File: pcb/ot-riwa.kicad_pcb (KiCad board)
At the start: 2 copper layers, 70 x 61.8 mm, 19 parts, among them IC2 RV-3028-C7, J1 USB4105-GF-A, U1 DPS368XTSA1, U2 MS88SF2, U3 MCP73831/OT, U4 AP2112K-3.3

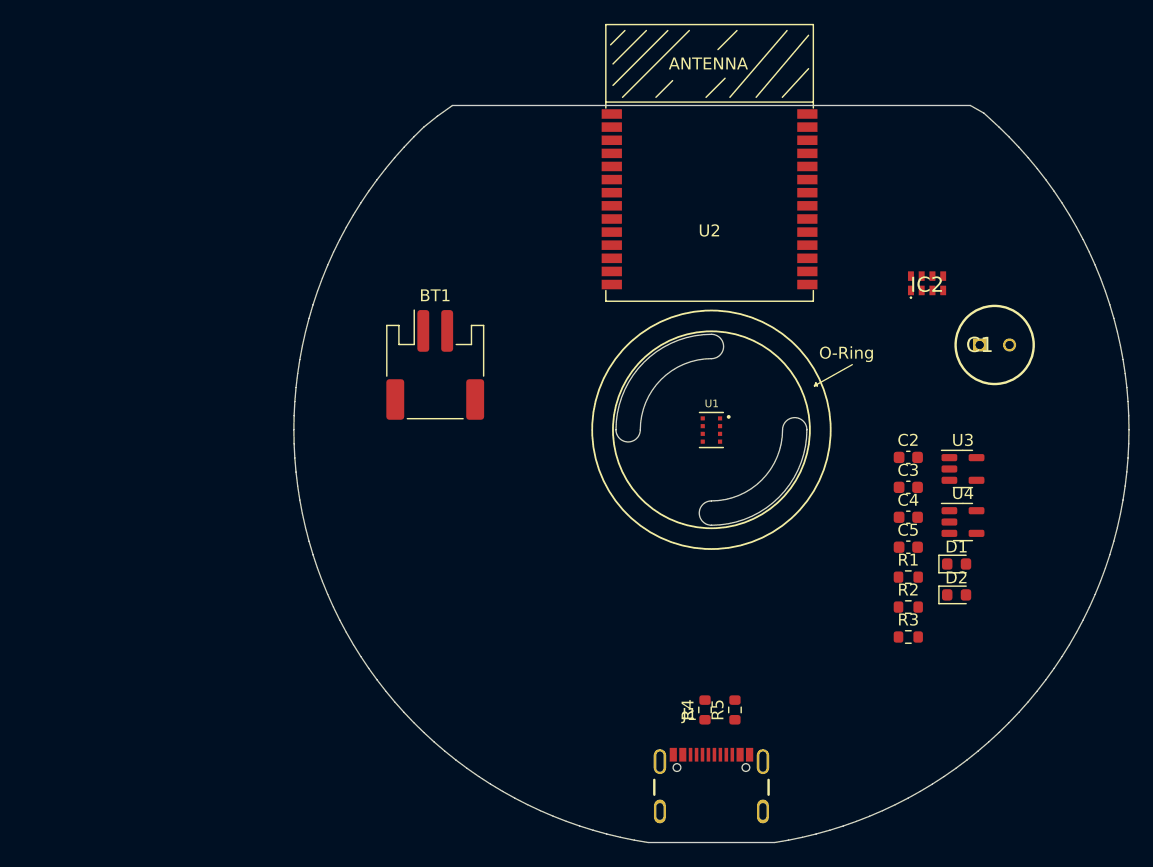
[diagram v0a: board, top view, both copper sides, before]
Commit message: Placed components on PCB Board (no layouting)
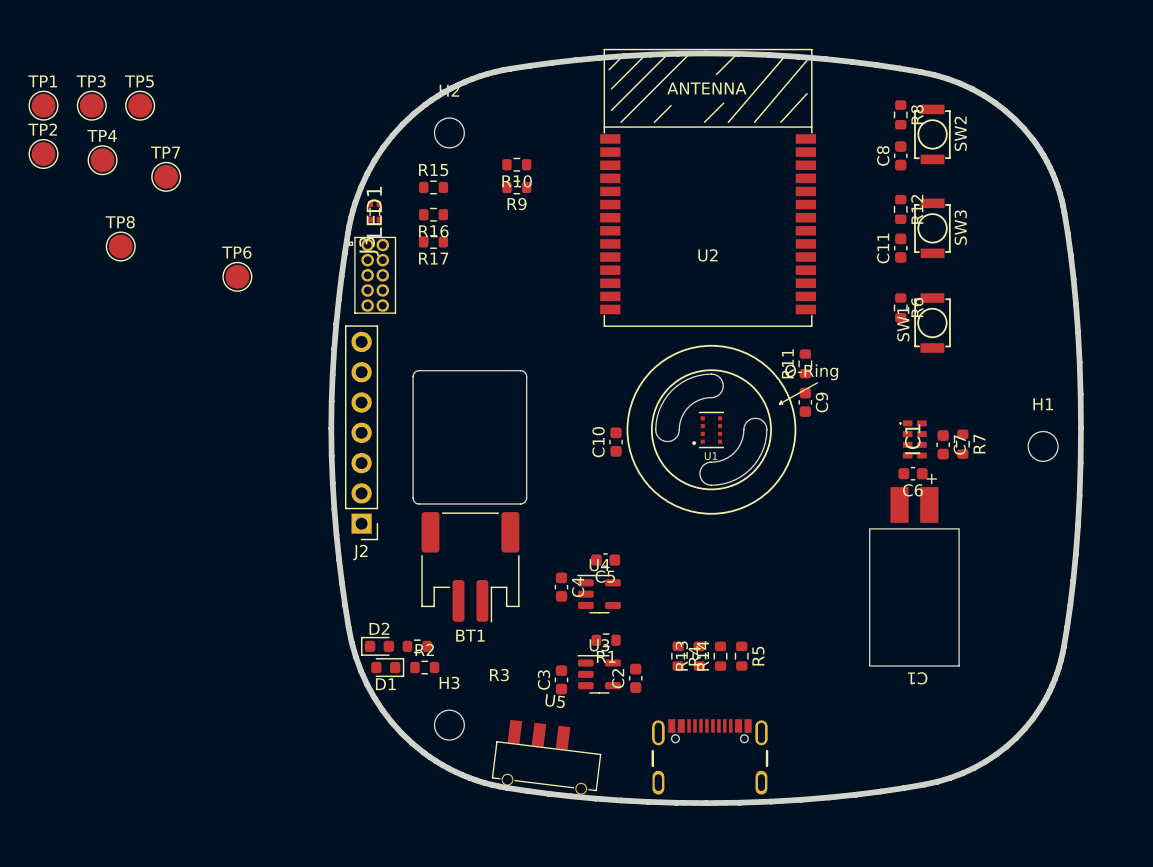
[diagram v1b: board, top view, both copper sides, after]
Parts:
- removed IC2: RV-3028-C7, RV-3028-C7:RV3028C732768kHz1ppmTAQC
- added C10: 0.1uF, Capacitor_SMD:C_0603_1608Metric, F.Cu at (128.3, 96.7)
- added C11: 0.1uF, Capacitor_SMD:C_0603_1608Metric, F.Cu at (152.1, 80.4)
- added C6: 0.1uF, Capacitor_SMD:C_0603_1608Metric, F.Cu at (153.2, 99.3)
- added C7: 0.1uF, Capacitor_SMD:C_0603_1608Metric, F.Cu at (155.7, 96.9)
- added C8: 0.1uF, Capacitor_SMD:C_0603_1608Metric, F.Cu at (152.1, 72.7)
- added C9: 0.1uF, Capacitor_SMD:C_0603_1608Metric, F.Cu at (144.1, 93.3)
- added G1: LOGO, LOGO, B.Cu at (136.3, 121.2)
- added H1: MountingHole, MountingHole:MountingHole_2.5mm, F.Cu at (164.1, 97.0)
- added H2: MountingHole, MountingHole:MountingHole_2.5mm, F.Cu at (114.3, 70.7)
- added H3: MountingHole, MountingHole:MountingHole_2.5mm, F.Cu at (114.3, 120.4)
- added IC1: RV-3028-C7, RV-3028-C7:RV3028C732768kHz1ppmTAQC, F.Cu at (153.3, 96.4)
- added J2: Conn_01x07_Pin, Connector_PinHeader_2.54mm:PinHeader_1x07_P2.54mm_Vertical, F.Cu at (106.9, 103.5)
- added J3: 62201021121, 62201021121:WURTH-1.27MM-PITCH-2WAY, F.Cu at (108.1, 82.7)
- added LED1: APHF1608LSEEQBDZGKC, APHF1608LSEEQBDZGKC:APHF1608LSEEQBDZGKC, F.Cu at (108.0, 77.4)
- added R10: 10k, Resistor_SMD:R_0603_1608Metric, F.Cu at (120.0, 73.4)
- added R11: 10k, Resistor_SMD:R_0603_1608Metric, F.Cu at (144.1, 90.1)
- added R12: 10k, Resistor_SMD:R_0603_1608Metric, F.Cu at (152.1, 77.2)
- added R13: 0R, Resistor_SMD:R_0603_1608Metric, F.Cu at (135.3, 114.6)
- added R14: 0R, Resistor_SMD:R_0603_1608Metric, F.Cu at (137.0, 114.6)
- added R15: 1k2, Resistor_SMD:R_0603_1608Metric, F.Cu at (113.0, 75.3)
- added R16: 2k2, Resistor_SMD:R_0603_1608Metric, F.Cu at (113.0, 77.6)
- added R17: 390R, Resistor_SMD:R_0603_1608Metric, F.Cu at (113.0, 79.9)
- added R6: 10k, Resistor_SMD:R_0603_1608Metric, F.Cu at (152.1, 85.4)
- added R7: 10k, Resistor_SMD:R_0603_1608Metric, F.Cu at (157.4, 96.8)
- added R8: 10k, Resistor_SMD:R_0603_1608Metric, F.Cu at (152.1, 69.2)
- added R9: 10k, Resistor_SMD:R_0603_1608Metric, F.Cu at (120.0, 75.3)
- added SW1: SKRKAEE020, SKRKAEE020:SKRKAEE020, F.Cu at (154.8, 86.7)
- added SW2: SKRKAEE020, SKRKAEE020:SKRKAEE020, F.Cu at (154.8, 70.9)
- added SW3: SKRKAEE020, SKRKAEE020:SKRKAEE020, F.Cu at (154.8, 78.7)
- added TP1: TP_3V3, TestPoint:TestPoint_Pad_D2.0mm, F.Cu at (80.3, 68.5)
- added TP2: TP_GND, TestPoint:TestPoint_Pad_D2.0mm, F.Cu at (80.3, 72.5)
- added TP3: TP_SDA, TestPoint:TestPoint_Pad_D2.0mm, F.Cu at (84.3, 68.5)
- added TP4: TP_SCK, TestPoint:TestPoint_Pad_D2.0mm, F.Cu at (85.2, 73.0)
- added TP5: TP_RTC_INT, TestPoint:TestPoint_Pad_D2.0mm, F.Cu at (88.4, 68.5)
- added TP6: TP_DPS_INT, TestPoint:TestPoint_Pad_D2.0mm, F.Cu at (96.5, 82.8)
- added TP7: TP_VBACKUP, TestPoint:TestPoint_Pad_D2.0mm, F.Cu at (90.6, 74.4)
- added TP8: TP_ENABLE, TestPoint:TestPoint_Pad_D2.0mm, F.Cu at (86.7, 80.3)
- added U5: 450405020524, 450405020524:450405020524, F.Cu at (122.3, 125.4)
- C1: footprint JUWT1105MCD:CAPPRD250W50D655H1050 -> JUWT1105MCD:supercap_horizontal
- moved D1 48.6 mm to (109.0, 115.6), turned to 180 degrees
- moved D2 48.6 mm to (108.4, 113.8)
- moved R3 41.2 mm to (111.6, 113.8), turned to 180 degrees
- moved R2 40.9 mm to (112.2, 115.6)
- moved U3 35.0 mm to (126.9, 116.1)
- moved C3 33.3 mm to (123.7, 116.6), turned to 90 degrees
- moved U4 31.1 mm to (126.9, 109.4)
- moved C4 29.7 mm to (123.7, 108.8), turned to -90 degrees
- moved C2 29.4 mm to (129.9, 116.5), turned to 90 degrees
- moved R1 25.9 mm to (127.4, 113.3), turned to 180 degrees
- moved C5 25.4 mm to (127.4, 106.6), turned to 180 degrees
- moved C1 18.2 mm to (153.5, 105.9), turned to 180 degrees
- moved BT1 17.2 mm to (116.1, 107.1), turned to 180 degrees
- moved R4 5.04 mm to (133.5, 114.6), turned to -90 degrees
- moved R5 4.54 mm to (138.8, 114.6), turned to -90 degrees
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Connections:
- net /main/USB_D+ renamed /main/MCU/USB_D+
- net /main/USB_D- renamed /main/MCU/USB_D-
- C1 pad 1: unconnected-(C1-+-Pad1) -> /main/RTC/VBackup
- C1 pad 2: unconnected-(C1---Pad2) -> GND
- U1 pad 1: Net-(U1-GND-Pad1) -> GND
- U1 pad 3: unconnected-(U1-SDI-Pad3) -> /main/SDA
- U1 pad 4: unconnected-(U1-SCK-Pad4) -> /main/SCK
- U1 pad 5: unconnected-(U1-SDO-Pad5) -> /main/DPS_INT
- U1 pad 6: unconnected-(U1-VDDIO-Pad6) -> +3.3V
- U1 pad 7: Net-(U1-GND-Pad1) -> GND
- U1 pad 8: unconnected-(U1-VDD-Pad8) -> +3.3V
- U2 pad 1: unconnected-(U2-GND-Pad1) -> GND
- U2 pad 10: unconnected-(U2-P0.08-Pad10) -> /main/MCU/LED_BLUE
- U2 pad 11: unconnected-(U2-P1.09-Pad11) -> /main/DPS_INT
- U2 pad 12: unconnected-(U2-P0.12-Pad12) -> /main/~{RTC_INT}
- U2 pad 13: unconnected-(U2-GND1-Pad13) -> GND
- U2 pad 14: unconnected-(U2-VCC-Pad14) -> +3.3V
- U2 pad 17: unconnected-(U2-SWDCLK-Pad17) -> /main/MCU/SWDCLK
- U2 pad 18: unconnected-(U2-SWDIO-Pad18) -> /main/MCU/SWDIO
- U2 pad 2: unconnected-(U2-P1.13-Pad2) -> /main/SCK
- U2 pad 22: unconnected-(U2-P0.20-Pad22) -> /main/MCU/BTN
- U2 pad 23: unconnected-(U2-P0.18/RST-Pad23) -> /main/MCU/RESET
- U2 pad 26: unconnected-(U2-D+-Pad26) -> /main/MCU/D+
- U2 pad 27: unconnected-(U2-D--Pad27) -> /main/MCU/D-
- U2 pad 28: unconnected-(U2-VDDH-Pad28) -> +3.3V
- U2 pad 3: unconnected-(U2-P1.15-Pad3) -> /main/SDA
- U2 pad 4: unconnected-(U2-P0.02-Pad4) -> /main/MCU/Rx
- U2 pad 5: unconnected-(U2-P0.29-Pad5) -> /main/MCU/Tx
- U2 pad 8: unconnected-(U2-P0.04-Pad8) -> /main/MCU/LED_RED
- U2 pad 9: unconnected-(U2-P0.06-Pad9) -> /main/MCU/LED_GREEN
- U4 pad 3: /main/ENABLE -> /main/PSU/ENABLE
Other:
- board size 70 x 61.8 mm -> 62.9 x 62.9 mm

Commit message: Replaces nRF52840 with ESP32-S3
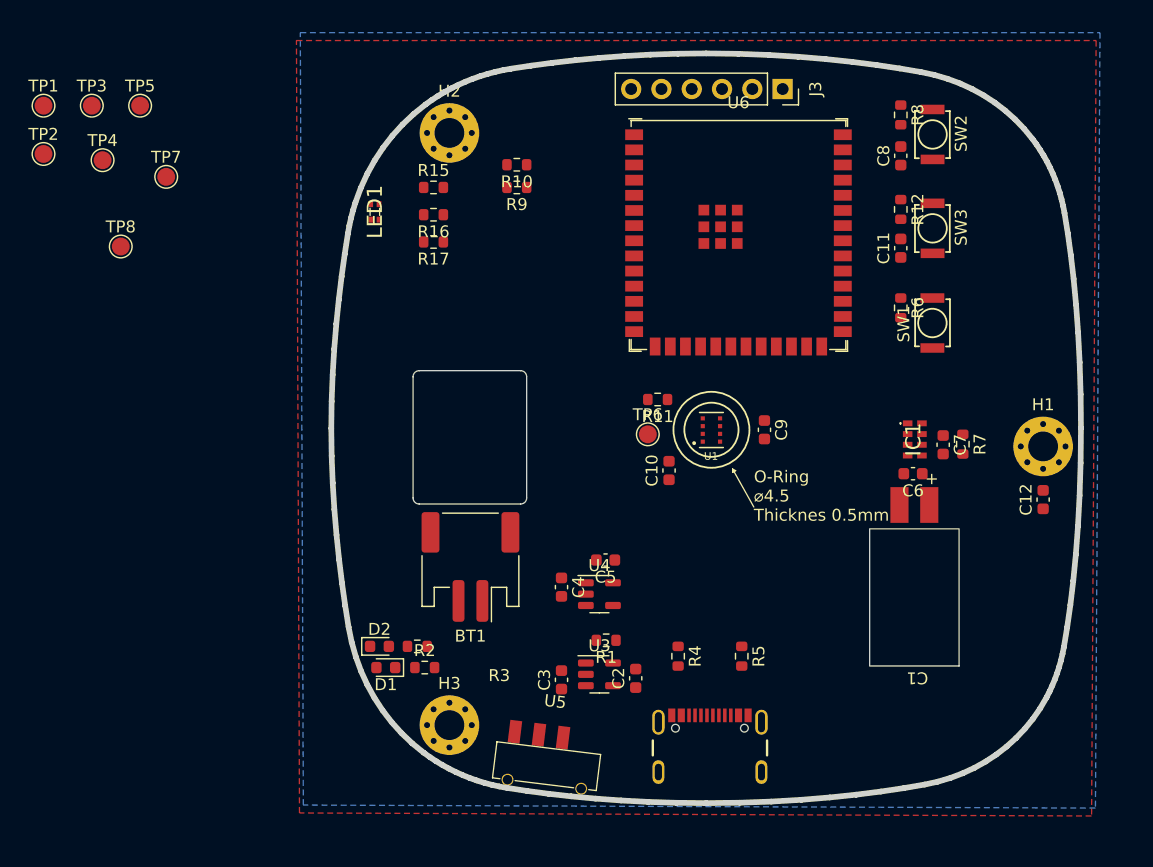
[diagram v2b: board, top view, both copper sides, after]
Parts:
- removed J2: Conn_01x07_Pin, Connector_PinHeader_2.54mm:PinHeader_1x07_P2.54mm_Vertical
- removed R13, R14: 0R, Resistor_SMD:R_0603_1608Metric
- removed U2: MS88SF2, MS88SF2:MS88SF2
- added C12: 0.1uF, Capacitor_SMD:C_0603_1608Metric, F.Cu at (164.1, 101.5)
- added U6: ESP32-S3-WROOM-1, ESP32-S3:ESP32-S3-WROOM-1U, F.Cu at (138.5, 79.2)
- H1, H2, H3: value MountingHole -> MountingHole_Pad; footprint MountingHole:MountingHole_2.5mm -> MountingHole:MountingHole_2.5mm_Pad_Via
- J3: value 62201021121 -> DNP; footprint 62201021121:WURTH-1.27MM-PITCH-2WAY -> Connector_PinSocket_2.54mm:PinSocket_1x06_P2.54mm_Vertical
- TP1, TP2, TP3, TP4, TP5, TP6, TP7, TP8: footprint TestPoint:TestPoint_Pad_D2.0mm -> TestPoint:TestPoint_Pad_D1.5mm
- moved J3 37.6 mm to (142.2, 67.1)
- moved TP6 36.9 mm to (130.9, 96.0)
- moved R11 12.7 mm to (131.8, 93.1), turned to 180 degrees
- moved C10 5.05 mm to (132.7, 99.0)
- moved C9 4.13 mm to (140.7, 95.6)
- moved J1 0.89 mm to (136.1, 124.3)
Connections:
- D1 pad 2: +BATT -> VBUS
- J3 pad 2: /main/MCU/SWDIO -> GND
- J3 pad 3: GND -> /main/MCU/Tx
- J3 pad 4: /main/MCU/SWDCLK -> /main/MCU/Rx
- J3 pad 5: GND -> /main/MCU/GPIO0
- J3 pad 6: unconnected-(J3-Pad6) -> /main/MCU/RESET
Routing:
- added copper zone on B.Cu, net GND
- added copper zone on F.Cu, net GND
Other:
- outline, holes or cut-outs redrawn
- board text added: "O-Ring ⌀4.5 Thicknes 0.5mm"
- board text removed: "O-Ring"

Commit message: Layout all components
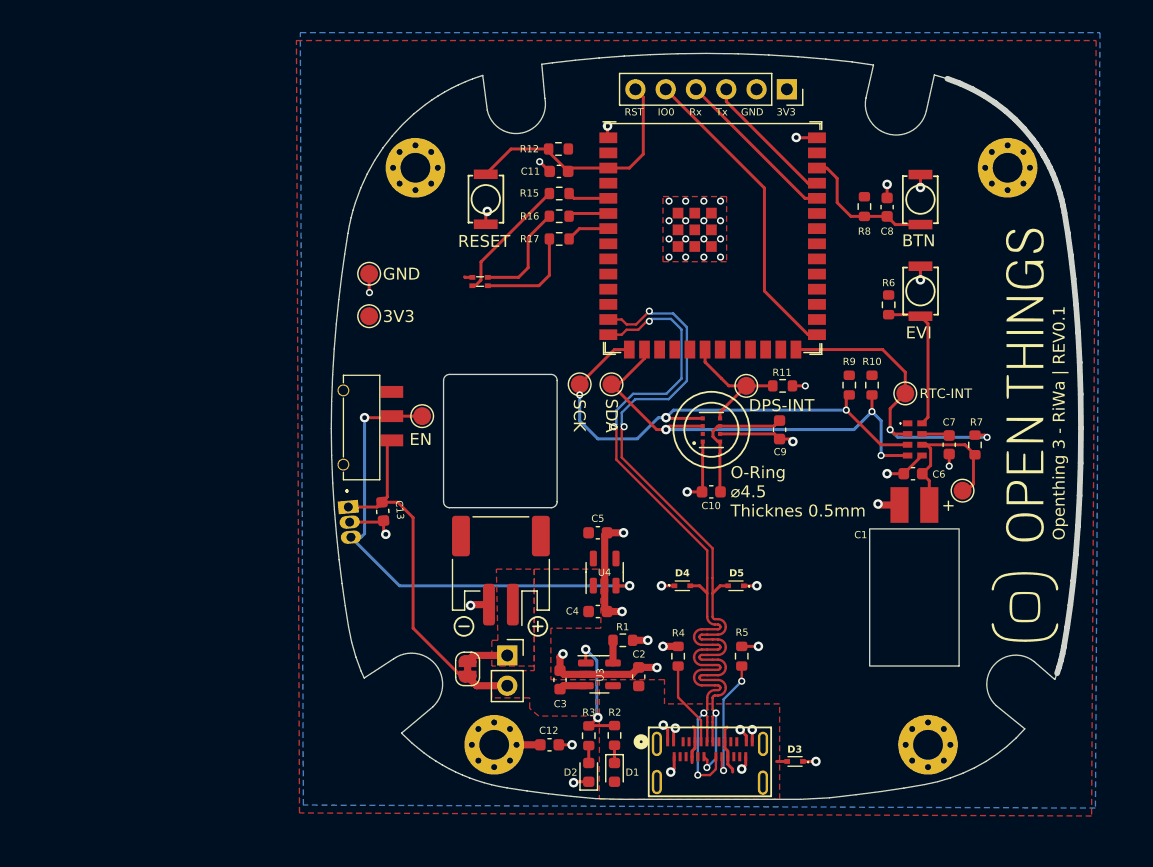
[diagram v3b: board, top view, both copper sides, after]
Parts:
- added C13: 0.1µF, Capacitor_SMD:C_0603_1608Metric, F.Cu at (108.7, 102.5)
- added D3: LESD5D5.0CT1G, LESD5D5.0CT1G:LESD5D50CT1G, F.Cu at (143.3, 123.4)
- added D4: LESD5D5.0CT1G, LESD5D5.0CT1G:LESD5D50CT1G, F.Cu at (133.8, 108.7)
- added D5: LESD5D5.0CT1G, LESD5D5.0CT1G:LESD5D50CT1G, F.Cu at (138.3, 108.7)
- added H4: MountingHole_Pad, MountingHole:MountingHole_2.5mm_Pad_Via, F.Cu at (154.4, 122.0)
- added IC2: DRV5032FB, DRV5032DULPGM:DRV5032DULPGM, F.Cu at (105.8, 102.1)
- added J2: DNP, Connector_PinSocket_2.54mm:PinSocket_1x02_P2.54mm_Vertical, F.Cu at (119.2, 114.6)
- added JP1: DNP, Jumper:SolderJumper-2_P1.3mm_Bridged_RoundedPad1.0x1.5mm, F.Cu at (115.8, 115.7)
- G1: moved to F.Cu
- J1: value USB4105-GF-A -> 124018612112A; footprint USB4105-GF-A:GCT_USB4105-GF-A -> 124018612112A:CONN_124018612112A_AMP
- moved TP7 71.8 mm to (157.3, 100.7)
- moved TP5 68.6 mm to (152.5, 92.6)
- moved H1 52.4 mm to (118.1, 122.0), turned to -90 degrees
- moved TP3 49.4 mm to (127.9, 91.8)
- moved H2 46.9 mm to (161.1, 73.7), turned to -90 degrees
- moved H3 46.8 mm to (111.5, 73.7), turned to -90 degrees
- moved C12 46.2 mm to (122.7, 122.0), turned to 0 degrees
- moved TP4 44.2 mm to (125.2, 91.8)
- moved SW3 37.5 mm to (117.3, 76.3), turned to -90 degrees
- moved G1 36.6 mm to (162.6, 95.6), turned to 90 degrees
- moved R10 35.0 mm to (149.7, 91.9), turned to 90 degrees
- moved U5 34.3 mm to (105.4, 95.5), turned to -90 degrees
- moved TP1 32.5 mm to (107.6, 86.1)
- moved R9 32.4 mm to (147.8, 91.9), turned to 90 degrees
- moved C11 29.4 mm to (123.5, 74.0), turned to 180 degrees
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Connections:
- BT1 pad 1: +BATT -> /main/PSU/BATTX+
- U6 pad 16: unconnected-(U6-GPIO46-Pad16) -> /main/SDA
- U6 pad 17: /main/MCU/LED_RED -> unconnected-(U6-GPIO9/TOUCH9/ADC1_CH8/FSPIHD/SUBSPIHD-Pad17)
- U6 pad 18: /main/MCU/LED_GREEN -> unconnected-(U6-GPIO10/TOUCH10/ADC1_CH9/FSPICS0/FSPIIO4/SUBSPICS0-Pad18)
- U6 pad 19: /main/MCU/LED_BLUE -> unconnected-(U6-GPIO11/TOUCH11/ADC2_CH0/FSPID/FSPIIO5/SUBSPID-Pad19)
- U6 pad 21: /main/~{RTC_INT} -> unconnected-(U6-GPIO13/TOUCH13/ADC2_CH2/FSPIQ/FSPIIO7/SUBSPIQ-Pad21)
- U6 pad 26: unconnected-(U6-GPIO45-Pad26) -> /main/~{RTC_INT}
- U6 pad 4: /main/SDA -> unconnected-(U6-GPIO4/TOUCH4/ADC1_CH3-Pad4)
- U6 pad 5: unconnected-(U6-GPIO5/TOUCH5/ADC1_CH4-Pad5) -> /main/MCU/LED_RED
- U6 pad 6: unconnected-(U6-GPIO6/TOUCH6/ADC1_CH5-Pad6) -> /main/MCU/LED_GREEN
- U6 pad 7: unconnected-(U6-GPIO7/TOUCH7/ADC1_CH6-Pad7) -> /main/MCU/LED_BLUE
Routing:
- net GND: track 0.00 -> 71.6 mm, vias 0 -> 50
- net /main/MCU/USB_D+: track 0.00 -> 71.2 mm, vias 0 -> 4
- net /main/MCU/USB_D-: track 0.00 -> 69.8 mm, vias 0 -> 4
- net /main/SCK: track 0.00 -> 43.2 mm, vias 0 -> 3
- net /main/PSU/ENABLE: track 0.00 -> 42.1 mm, vias 0 -> 2
- net /main/SDA: track 0.00 -> 39.3 mm, vias 0 -> 3
- net +BATT: track 0.00 -> 33.1 mm
- net /main/~{RTC_INT}: track 0.00 -> 26.4 mm, vias 0 -> 2
- net /main/MCU/GPIO0: track 0.00 -> 26.3 mm
- net /main/MCU/RESET: track 0.00 -> 21.3 mm
- net +3.3V: track 0.00 -> 14.4 mm
- net /main/RTC/VBackup: track 0.00 -> 14.4 mm
- net /main/MCU/Rx: track 0.00 -> 13.9 mm
- net /main/RTC/EVI: track 0.00 -> 12.2 mm
- net /main/MCU/BTN: track 0.00 -> 11.8 mm
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- added copper zone on F.Cu, net +3.3V
- added copper zone on F.Cu, net +BATT
- added copper zone on F.Cu, net /main/PSU/BATTX+
- added copper zone on F.Cu, net VBUS
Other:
- board size 62.9 x 62.9 mm -> 62.9 x 62.5 mm
- board text added: "3V3"
- board text added: "BTN"
- board text added: "DPS-INT"
- board text added: "EN"
- board text added: "EVI"
- board text added: "GND"
- board text added: "IO0"
- board text added: "Openthing 3 - RiWa | REV0.1"
- board text added: "RESET"
- board text added: "RST"
- board text added: "RTC-INT"
- board text added: "Rx"
- board text added: "SCK"
- board text added: "SDA"
- board text added: "Tx"

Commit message: Refactored layout + silkscreen + added I2C connector
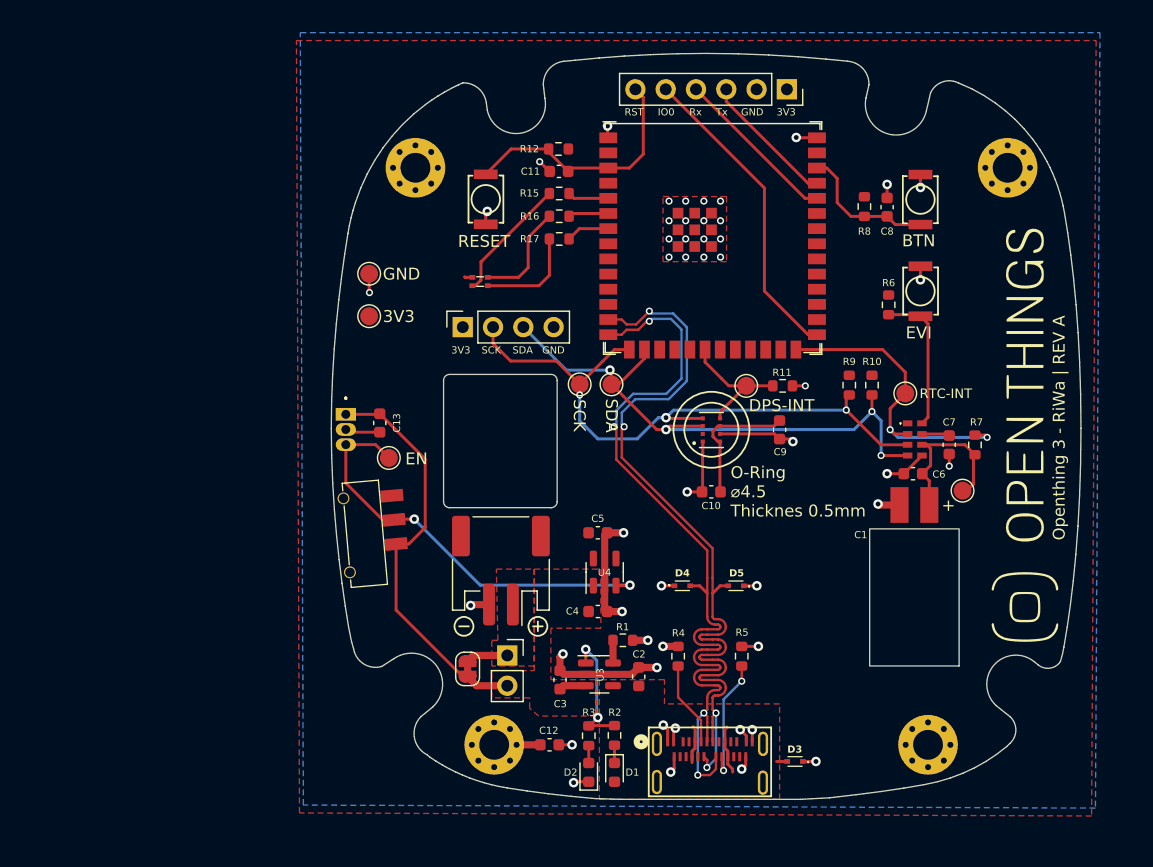
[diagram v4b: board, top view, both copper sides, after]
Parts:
- added J4: Conn_01x04_Pin, Connector_PinSocket_2.54mm:PinSocket_1x04_P2.54mm_Vertical, F.Cu at (115.4, 87.0)
- moved U5 9.05 mm to (105.7, 104.5), turned to -85 degrees
- moved IC2 7.78 mm to (105.6, 94.3), turned to 90 degrees
- moved C13 7.42 mm to (108.5, 95.1), turned to -90 degrees
- moved TP8 4.48 mm to (109.2, 98.0)
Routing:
- net /main/SCK: track 43.2 -> 53.3 mm
- net /main/SDA: track 39.3 -> 49.3 mm, vias 3 -> 4
- net /main/PSU/ENABLE: track 42.1 -> 35.9 mm
- net +BATT: track 33.1 -> 36.8 mm
- net GND: track 71.6 -> 70.4 mm, vias 50 -> 49
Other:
- outline, holes or cut-outs redrawn
- board text added: "Openthing 3 - RiWa | REV A"
- board text removed: "Openthing 3 - RiWa | REV0.1"
